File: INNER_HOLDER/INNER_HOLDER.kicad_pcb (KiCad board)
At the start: 2 copper layers, 10 x 30 mm, 1 part

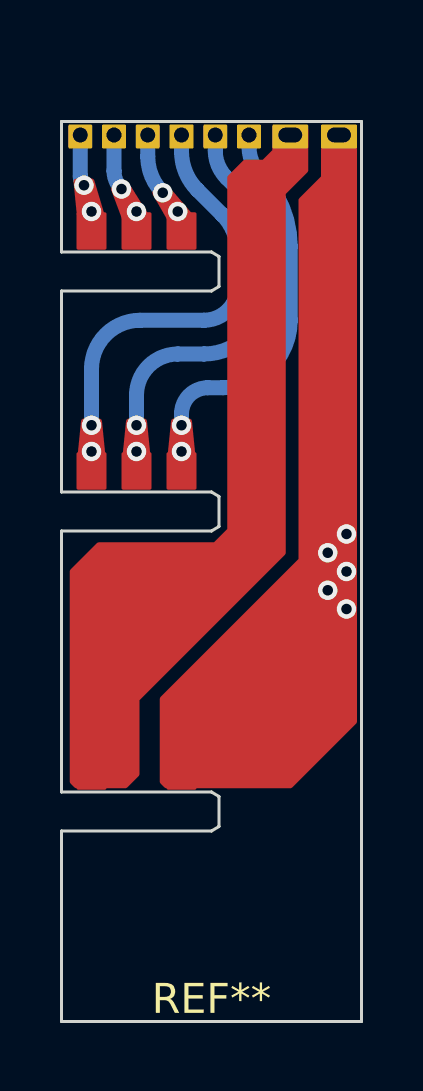
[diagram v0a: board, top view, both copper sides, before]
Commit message: Add OUTER_HOLDER and update INNER_HOLDER.
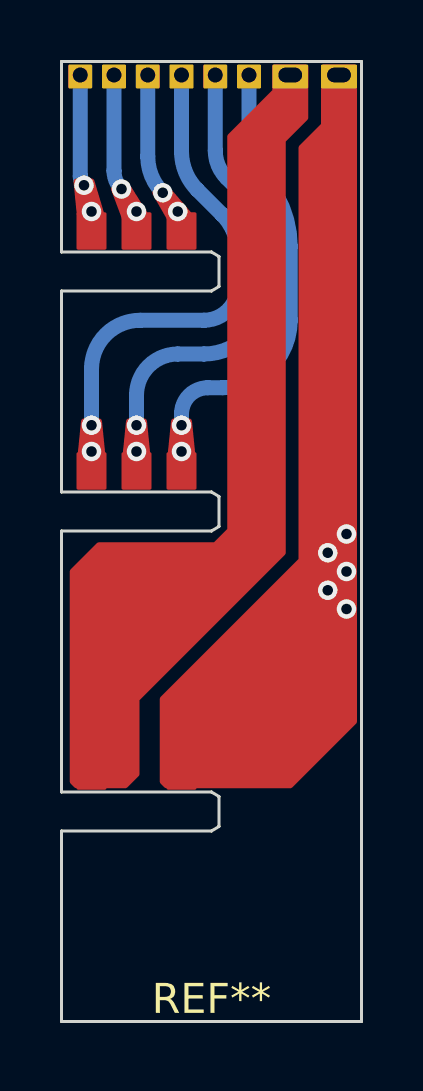
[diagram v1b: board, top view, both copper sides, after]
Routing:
- net (no net): track 49.8 -> 61.8 mm
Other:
- board size 10 x 30 mm -> 10 x 32 mm
